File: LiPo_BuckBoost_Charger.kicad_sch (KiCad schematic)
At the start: 53 parts, among them J2 Type-C_6P, J3 Conn_01x01, J4 Conn_01x01, J6 Conn_01x01, J7 Conn_01x01, J7 JST PH Connector, U1 TP4056, U2 DW01A, U3 FS8205A, U4 TPS63020

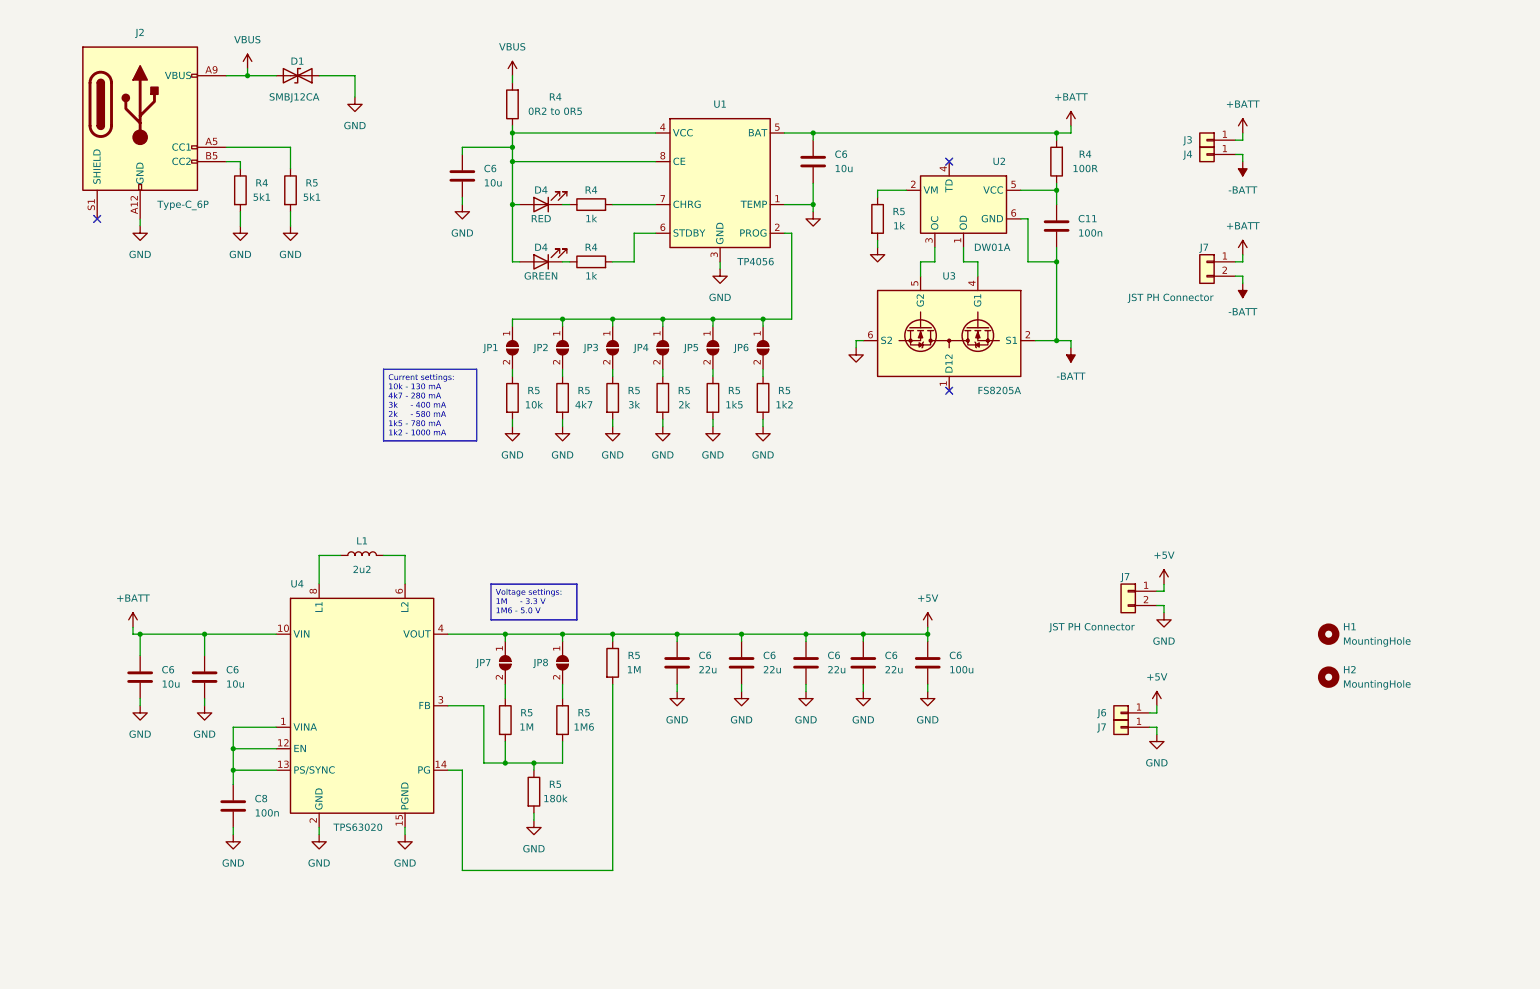
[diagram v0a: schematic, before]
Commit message: Pcb traces and layout done
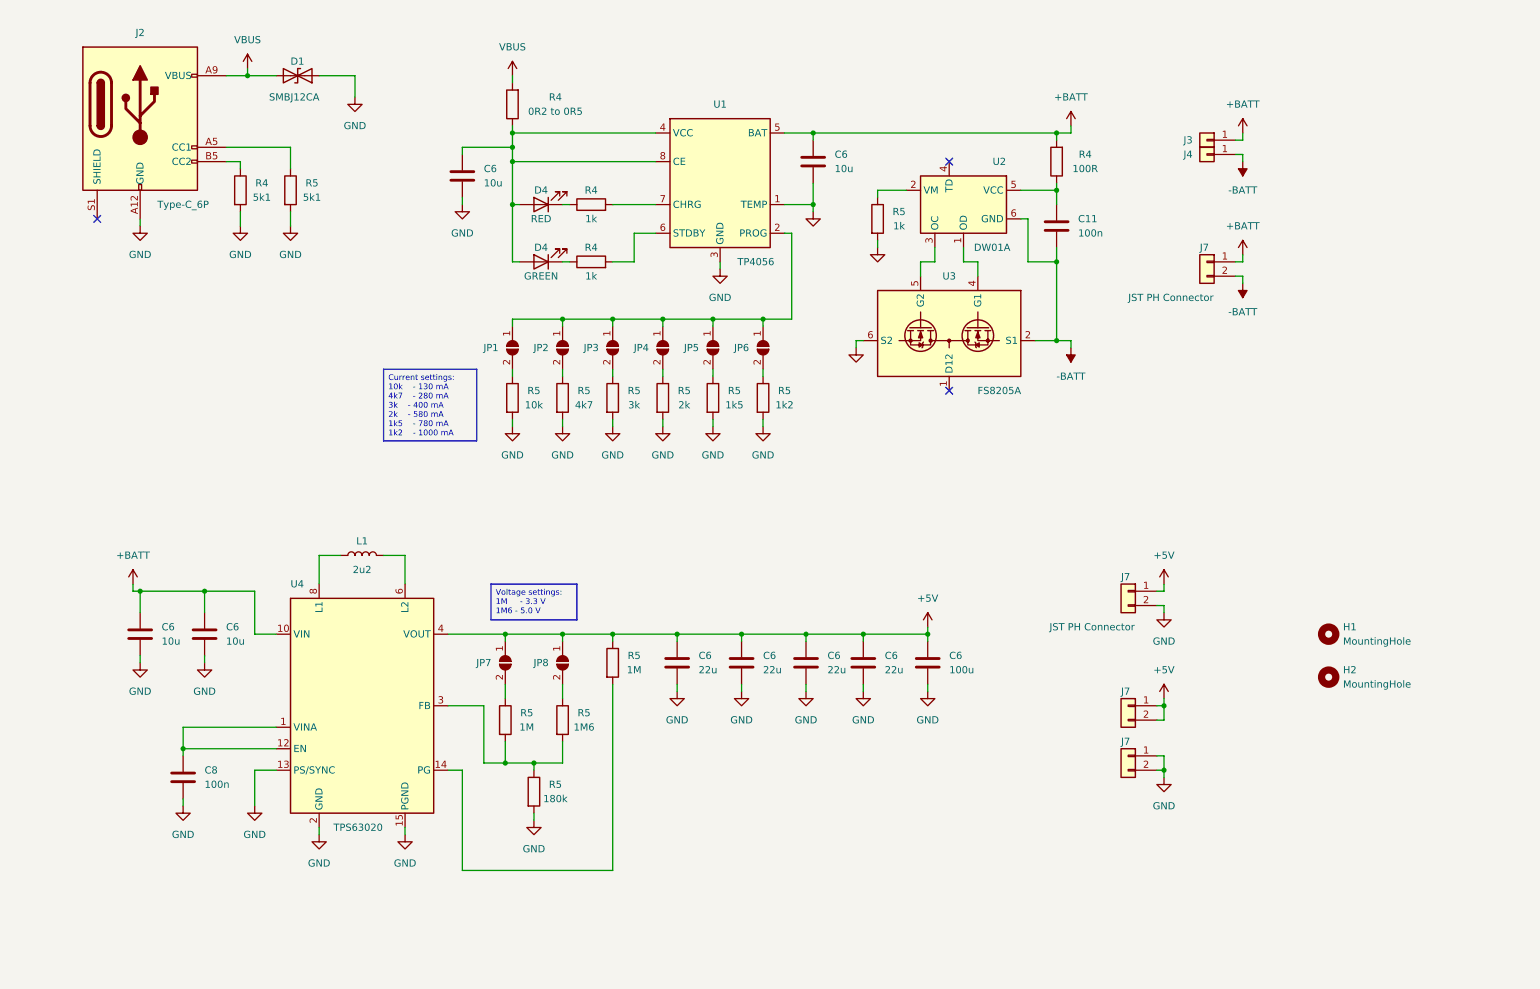
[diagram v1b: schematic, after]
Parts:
- removed J6, J7: Conn_01x01, Connector_PinHeader_2.54mm:PinHeader_1x01_P2.54mm_Vertical, symbol Connector_Generic:Conn_01x01
- added J7 (x2): JST PH Connector, Connector_PinHeader_2.54mm:PinHeader_1x02_P2.54mm_Vertical, symbol Connector_Generic:Conn_01x02
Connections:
- net +5V: now also J7.1 (Pin_1), J7.2 (Pin_2)
- net GND: now also U4.13 (PS/SYNC), J7.1 (Pin_1), J7.2 (Pin_2)
- net at C8.1, U4.1 (VINA), U4.12 (EN): no longer U4.13 (PS/SYNC)
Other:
- moved on the sheet: C6, C8

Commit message: schematic update, added imgs
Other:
- note added: "Connectors"
- note added: "TP4056 LiPo Charger with DW01A Protection IC"
- note added: "TPS63020 Buck-Boost Converter"
- note added: "Type C Connector"
- company: (none) -> Potpurri
- title: (none) -> LiPo Buck-Boost Charger
- moved on the sheet: C11, C6, C8, D1, D4, H1, H2, J2, J3, J4, J7, JP1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

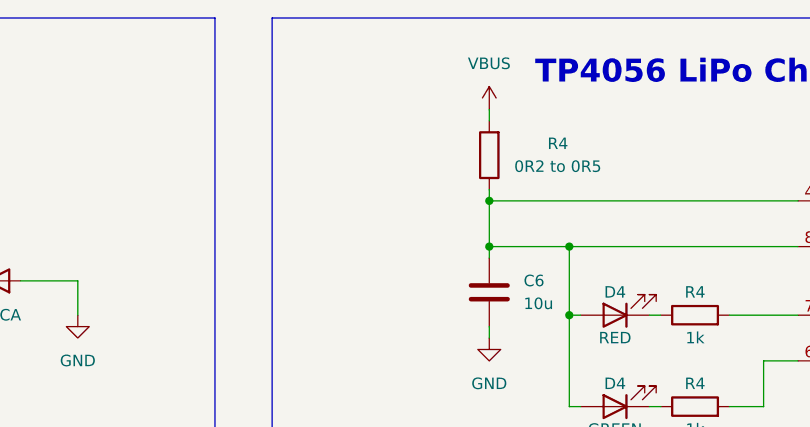
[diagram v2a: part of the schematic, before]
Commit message: Version 1.1 - added 2512 footprint for input resistor to TP4056
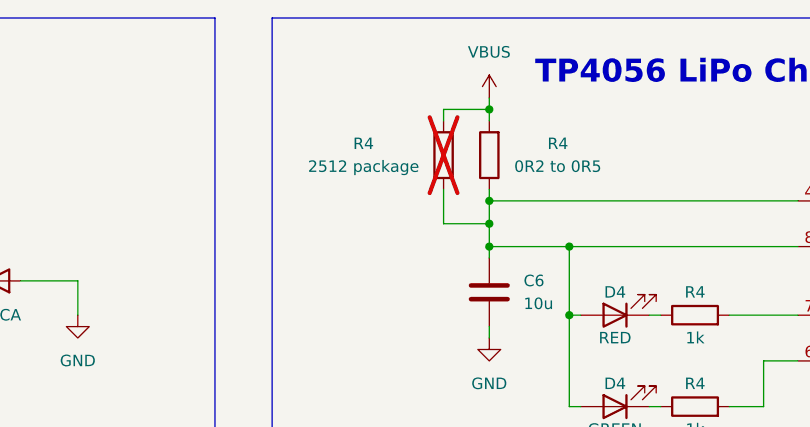
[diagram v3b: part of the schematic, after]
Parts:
- added R4: 2512 package, Resistor_SMD:R_2512_6332Metric, symbol Device:R
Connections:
- net VBUS: now also R4.2
- net at C6.1, D4.2 (A), D4.2 (A)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: now also R4.1
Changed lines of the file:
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@@
   (title_block
     (title "LiPo Buck-Boost Charger")
-    (rev "1.0")
+    (rev "1.1")
     (company "Potpurri")
   )
@@
   (junction (at 168.91 74.93) (diameter 0) (color 0 0 0 0)
   )
+  (junction (at 124.46 31.75) (diameter 0) (color 0 0 0 0)
+  )
   (junction (at 96.52 166.37) (diameter 0) (color 0 0 0 0)
   )
@@
   )
   (junction (at 34.29 163.83) (diameter 0) (color 0 0 0 0)
+  )
+  (junction (at 124.46 44.45) (diameter 0) (color 0 0 0 0)
   )
   (junction (at 166.37 143.51) (diameter 0) (color 0 0 0 0)
@@
     (stroke (width 0) (type default))
   )
-  (wire (pts (xy 124.46 41.91) (xy 124.46 46.99))
+  (wire (pts (xy 124.46 41.91) (xy 124.46 44.45))
     (stroke (width 0) (type default))
   )
@@
     (stroke (width 0) (type default))
   )
+  (wire (pts (xy 119.38 31.75) (xy 124.46 31.75))
+    (stroke (width 0) (type default))
+  )
   (wire (pts (xy 26.67 139.7) (xy 26.67 135.89))
     (stroke (width 0) (type default))
@@
     (stroke (width 0) (type default))
   )
+  (wire (pts (xy 119.38 33.02) (xy 119.38 31.75))
+    (stroke (width 0) (type default))
+  )
   (wire (pts (xy 24.13 135.89) (xy 26.67 135.89))
     (stroke (width 0) (type default))
@@
     (stroke (width 0) (type default))
   )
+  (wire (pts (xy 124.46 30.48) (xy 124.46 31.75))
+    (stroke (width 0) (type default))
+  )
   (wire (pts (xy 234.95 152.4) (xy 234.95 149.86))
     (stroke (width 0) (type default))
@@
     (stroke (width 0) (type default))
   )
+  (wire (pts (xy 119.38 44.45) (xy 124.46 44.45))
+    (stroke (width 0) (type default))
+  )
   (wire (pts (xy 186.69 41.91) (xy 229.87 41.91))
     (stroke (width 0) (type default))
@@
     (stroke (width 0) (type default))
   )
+  (wire (pts (xy 119.38 40.64) (xy 119.38 44.45))
+    (stroke (width 0) (type default))
+  )
   (wire (pts (xy 96.52 175.26) (xy 96.52 176.53))
     (stroke (width 0) (type default))
@@
   )
   (wire (pts (xy 151.13 74.93) (xy 151.13 76.2))
+    (stroke (width 0) (type default))
+  )
+  (wire (pts (xy 124.46 44.45) (xy 124.46 46.99))
     (stroke (width 0) (type default))
   )
@@
     )
   )
-  (symbol (lib_id "power:VBUS") (at 124.46 31.75 0) (unit 1)
-    (in_bom yes) (on_board yes) (dnp no) (fields_autoplaced)
-    (property "Reference" "#PWR06" (at 124.46 35.56 0)
-      (effects (font (size 1.27 1.27)) hide)
-    )
-    (property "Value" "VBUS" (at 124.46 26.67 0)
-      (effects (font (size 1.27 1.27)))
-    )
-    (property "Footprint" "" (at 124.46 31.75 0)
-      (effects (font (size 1.27 1.27)) hide)
-    )
-    (property "Datasheet" "" (at 124.46 31.75 0)
+  (symbol (lib_id "power:VBUS") (at 124.46 30.48 0) (unit 1)
+    (in_bom yes) (on_board yes) (dnp no) (fields_autoplaced)
+    (property "Reference" "#PWR06" (at 124.46 34.29 0)
+      (effects (font (size 1.27 1.27)) hide)
+    )
+    (property "Value" "VBUS" (at 124.46 25.4 0)
+      (effects (font (size 1.27 1.27)))
+    )
+    (property "Footprint" "" (at 124.46 30.48 0)
+      (effects (font (size 1.27 1.27)) hide)
+    )
+    (property "Datasheet" "" (at 124.46 30.48 0)
       (effects (font (size 1.27 1.27)) hide)
     )
@@
         )
       )
+    )
+  )
+  (symbol (lib_id "Device:R") (at 119.38 36.83 180) (unit 1)
+    (in_bom yes) (on_board yes) (dnp yes)
+    (property "Reference" "R4" (at 110.49 35.56 0)
+      (effects (font (size 1.27 1.27)))
+    )
+    (property "Value" "2512 package" (at 110.49 38.1 0)
+      (effects (font (size 1.27 1.27)))
+    )
+    (property "Footprint" "Resistor_SMD:R_2512_6332Metric" (at 121.158 36.83 90)
+      (effects (font (size 1.27 1.27)) hide)
+    )
+    (property "Datasheet" "~" (at 119.38 36.83 0)
+      (effects (font (size 1.27 1.27)) hide)
+    )
+    (pin "1")
+    (pin "2")
+    (instances
+      (project "VattirBoard_4layer"
+        (path "/a72e996f-55bb-4228-9f30-6f8d77e04e24"
+          (reference "R4") (unit 1)
+        )
+      )
+      (project "LiPo_BuckBoost_Charger"
+        (path "/ebf16ca0-689c-447d-aaab-3c694dddd46d"
+          (reference "R18") (unit 1)
+        )
+      )

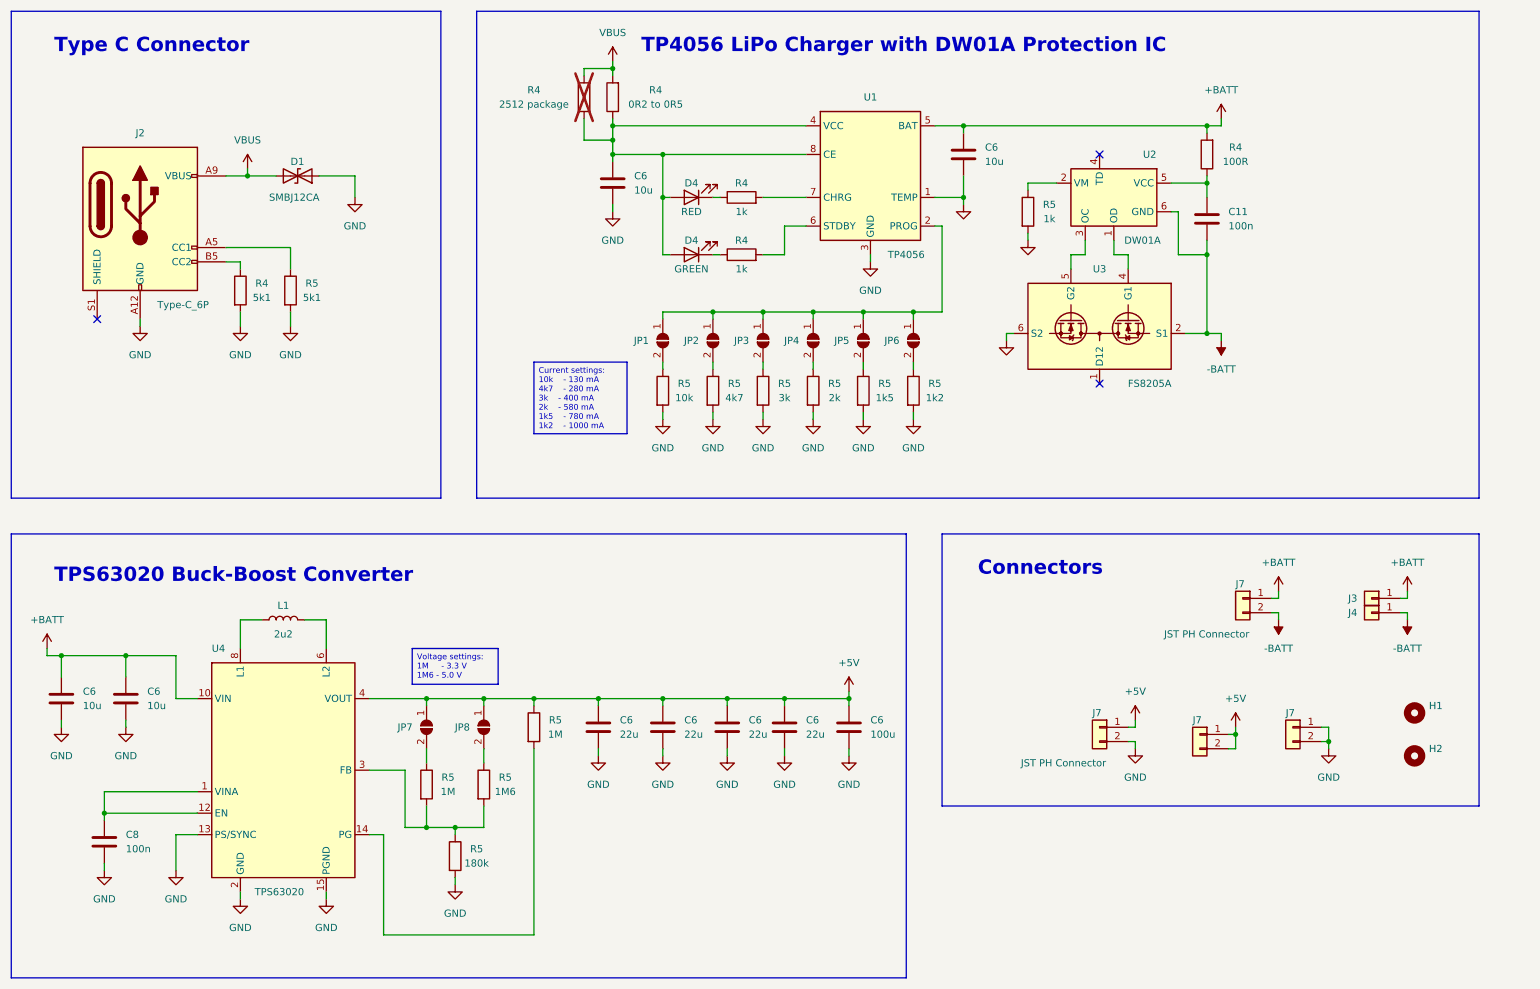
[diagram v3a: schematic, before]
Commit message: added pmos circuit to disconnect battery from load during charging
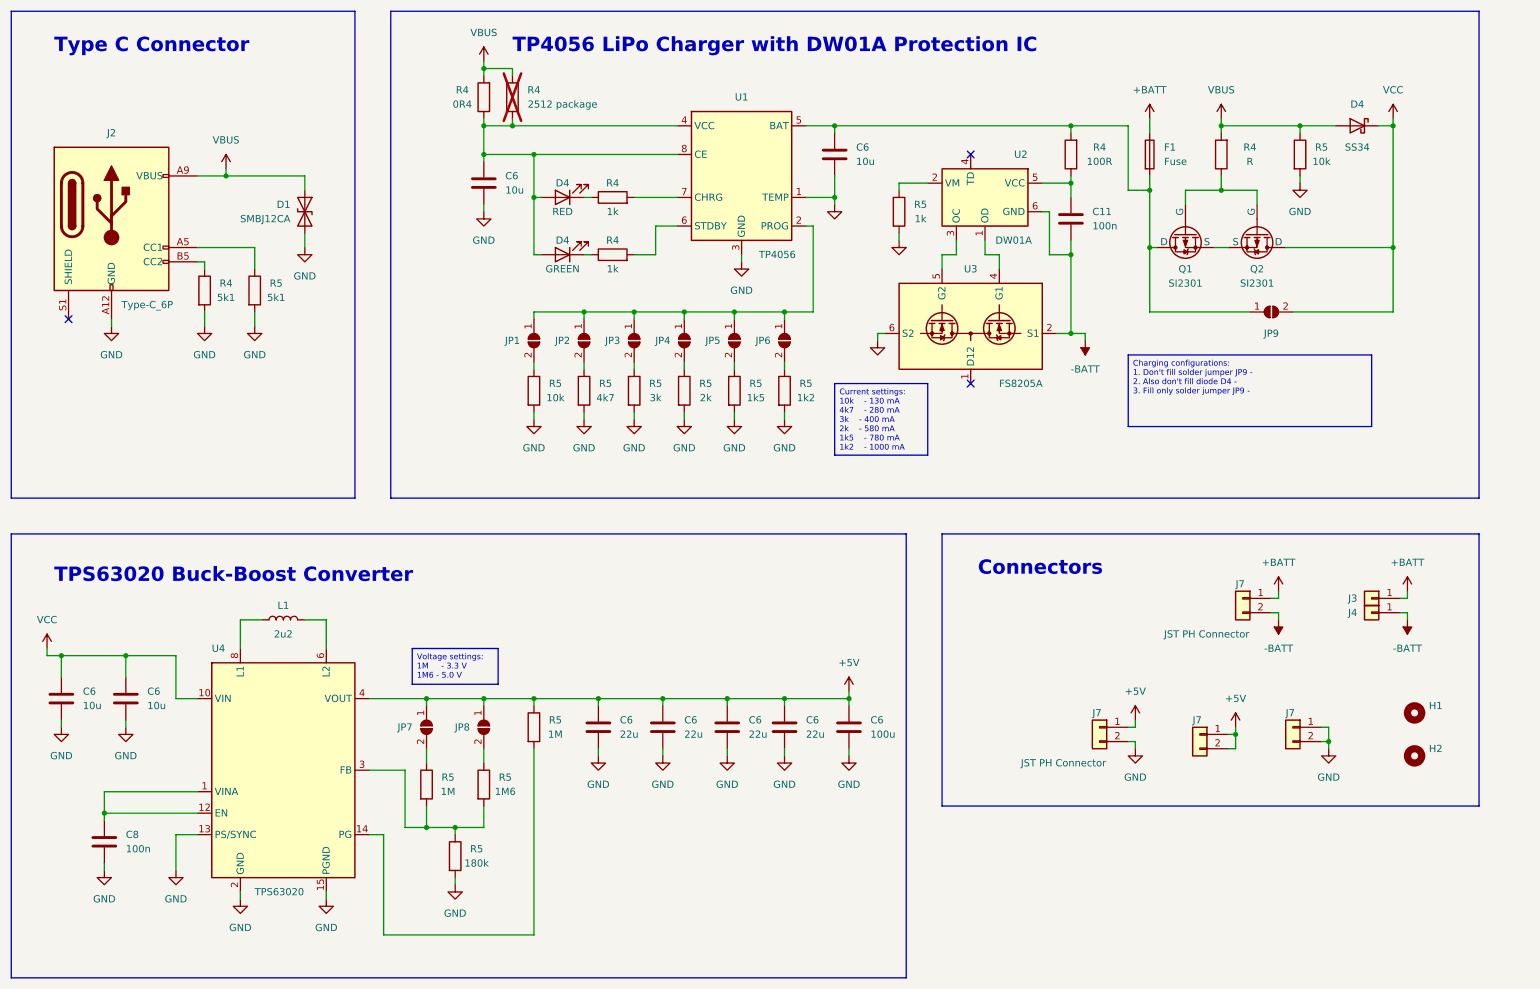
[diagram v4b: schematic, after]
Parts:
- removed R4: 0R2 to 0R5, Resistor_SMD:R_0805_2012Metric, symbol Device:R
- added D4: SS34, Diode_SMD:D_SMA, symbol Device:D_Schottky
- added F1: Fuse, symbol Device:Fuse
- added JP9: SolderJumper_2_Open, Jumper:SolderJumper-2_P1.3mm_Open_TrianglePad1.0x1.5mm, symbol Jumper:SolderJumper_2_Open
- added Q1, Q2: SI2301, Package_TO_SOT_SMD:SOT-23, symbol Simulation_SPICE:PMOS
- added R4: R, Resistor_SMD:R_0805_2012Metric, symbol Device:R
- added R4: 0R4, Resistor_SMD:R_0805_2012Metric, symbol Device:R
- added R5: 10k, Resistor_SMD:R_0805_2012Metric, symbol Device:R
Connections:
- net +BATT: now also F1.1; no longer C6.1, C6.1, C6.1, R4.2, U1.5 (BAT), U4.10 (VIN), U4.11 (VIN)
- net GND: now also D1.2 (A2), R5.2; no longer D1.1 (A1)
- net VBUS: now also D1.1 (A1), D4.2 (A), R4.2, R4.2, R5.1; no longer D1.2 (A2)
- net at C6.1, D4.2 (A), D4.2 (A)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: now also R4.1
- new net: C6.1, F1.2, JP9.1 (A), Q1.1 (D), R4.2, U1.5 (BAT)
- new net: Q1.2 (G), Q2.2 (G), R4.1
- new net: Q1.3 (S), Q2.3 (S)
- new net VCC: C6.1, C6.1, D4.1 (K), JP9.2 (B), Q2.1 (D), U4.10 (VIN), U4.11 (VIN)
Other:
- moved on the sheet: C11, C6, D4, J2, JP1, JP2, JP3, JP4, JP5, JP6, R4, R5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
